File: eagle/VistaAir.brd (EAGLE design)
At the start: 97.3 x 54.6 mm, 12 parts

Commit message: fix manual routing short
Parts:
- moved B3 1.24 mm to (67.8, 36.2)
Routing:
- net BOARD_GND: track 148.1 -> 125.3 mm, vias 0 -> 2
- net 3V3: track 39.8 -> 41.6 mm
- net PWM1_5V: track 31.9 -> 30.6 mm
- net CLW2_5V: track 30.9 -> 29.7 mm
- net PWM2_5V: track 37.6 -> 36.4 mm
- net CLW1_5V: track 38.3 -> 37.1 mm
- net CLW2_3V3: track 9.40 -> 9.91 mm

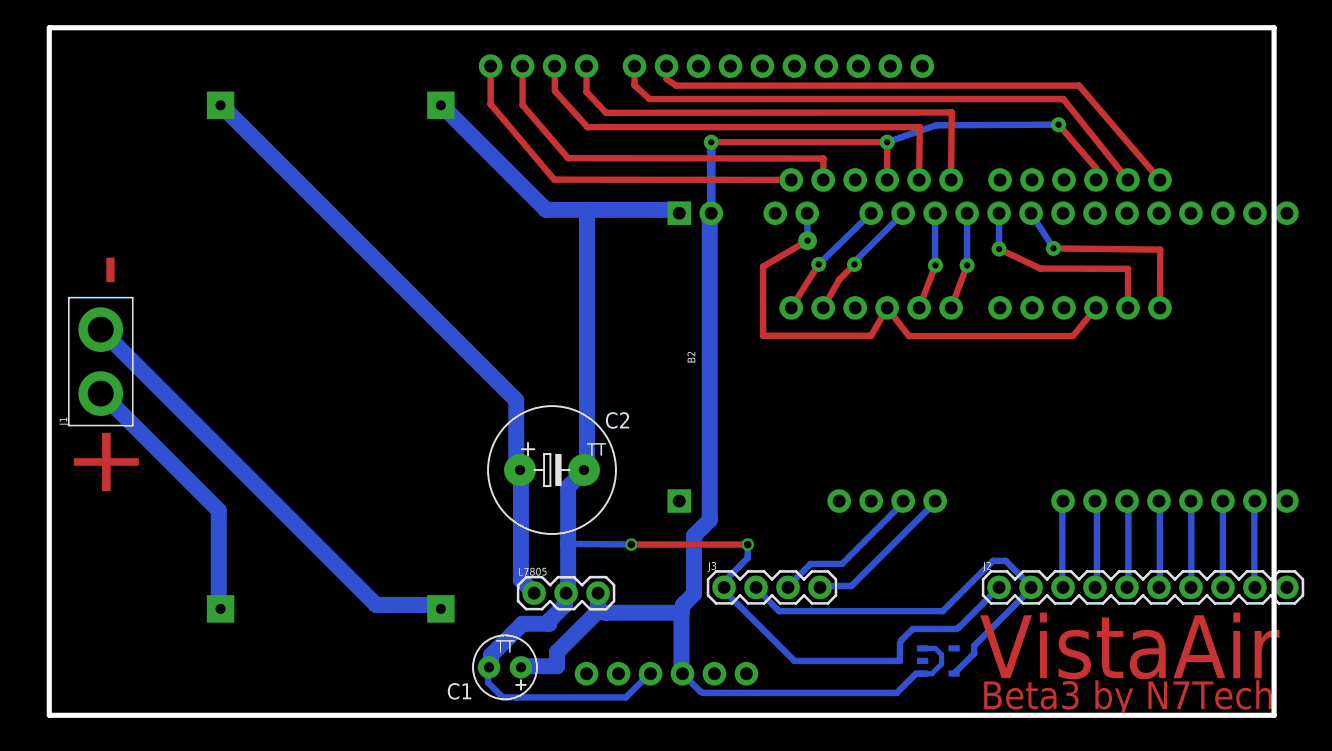
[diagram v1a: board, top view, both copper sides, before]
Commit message: managed to break ground connection to 3.6v regulator again - fixed it
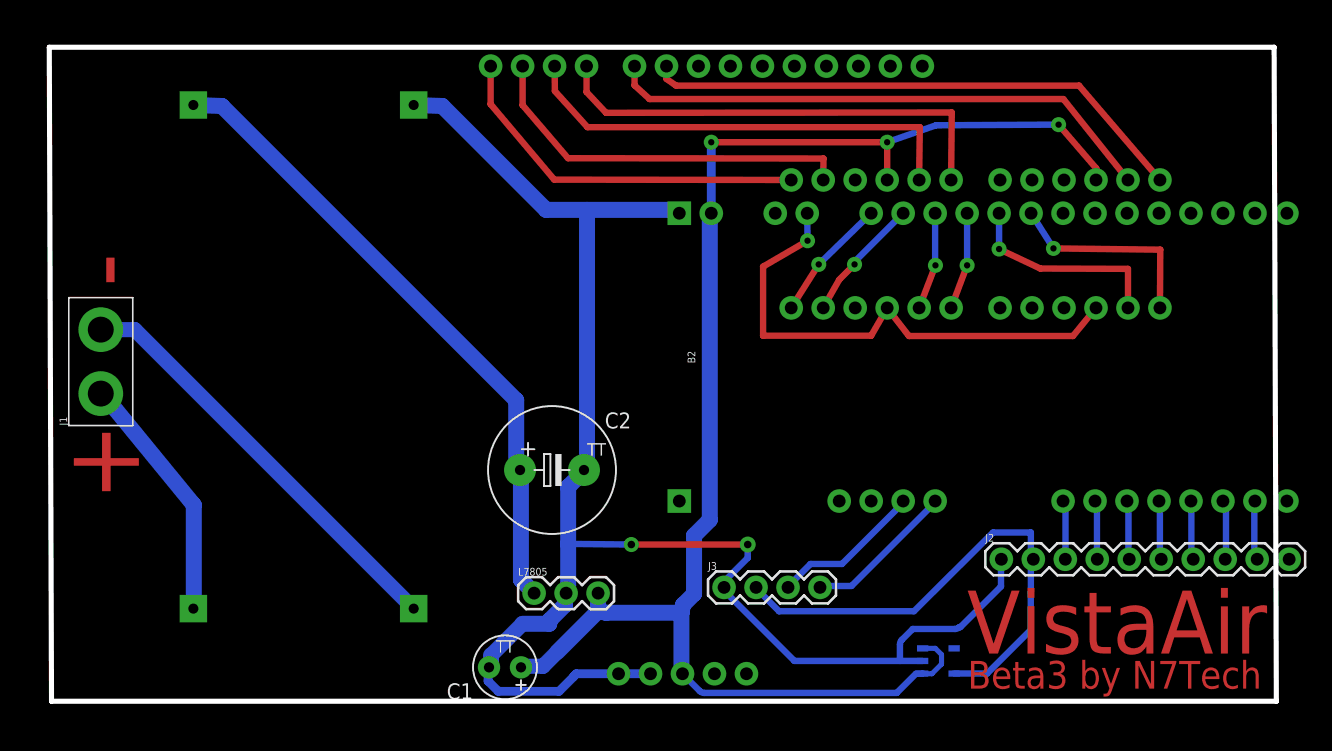
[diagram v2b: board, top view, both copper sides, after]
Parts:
- moved J2 2.24 mm to (78.2, 11.1)
- moved U$2 2.16 mm to (22.7, 27.2)
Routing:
- net 3V6: track 34.6 -> 40.7 mm
- net BOARD_GND: track 125.3 -> 131.4 mm
- net ENC1B: track 6.98 -> 4.67 mm
- net LIMTOPA: track 6.93 -> 4.66 mm
- net GND12: track 36.3 -> 34.0 mm
- net LIMTOPB: track 6.89 -> 4.67 mm
- net ENC1A: track 6.88 -> 4.69 mm
- net LIMBOTA: track 6.86 -> 4.69 mm
- net 5V5: track 49.0 -> 51.2 mm
- net LIMBOTB: track 6.86 -> 4.74 mm
- net LED: track 6.87 -> 4.76 mm
- net V12: track 21.0 -> 19.8 mm
- net V5IN: track 120.2 -> 119.6 mm
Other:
- board size 97.3 x 54.6 mm -> 97.5 x 51.9 mm

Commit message: board tidy up, encoders working with modified library
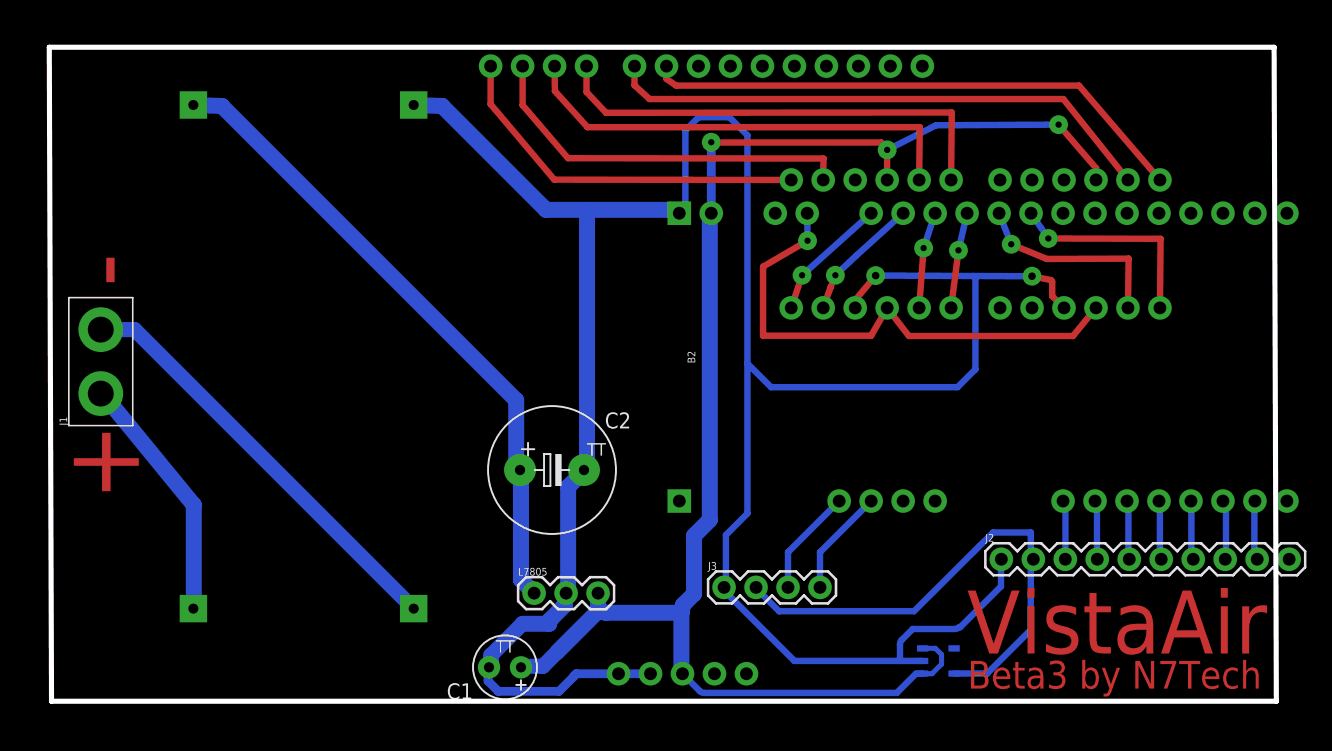
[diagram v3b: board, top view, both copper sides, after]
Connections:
- removed net N$1: B3.GND1
- removed net N$2: B3.GND2
- removed net N$3: B4.GND1
- removed net N$4: B4.GND2
- removed net NC1: B2.35
- removed net NC2: B2.34
- new net GND: B3.GND2, B4.GND2
- net BOARD_GND: now also B3.GND1, B4.GND1
- net ENC2A: now also B2.35; no longer B2.33
- net ENC2B: now also B2.34; no longer B2.32
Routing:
- net BOARD_GND: track 131.4 -> 209.0 mm
- net ENC2A: track 12.1 -> 8.54 mm
- net ENC2B: track 12.0 -> 8.54 mm

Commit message: board now with working logic converter
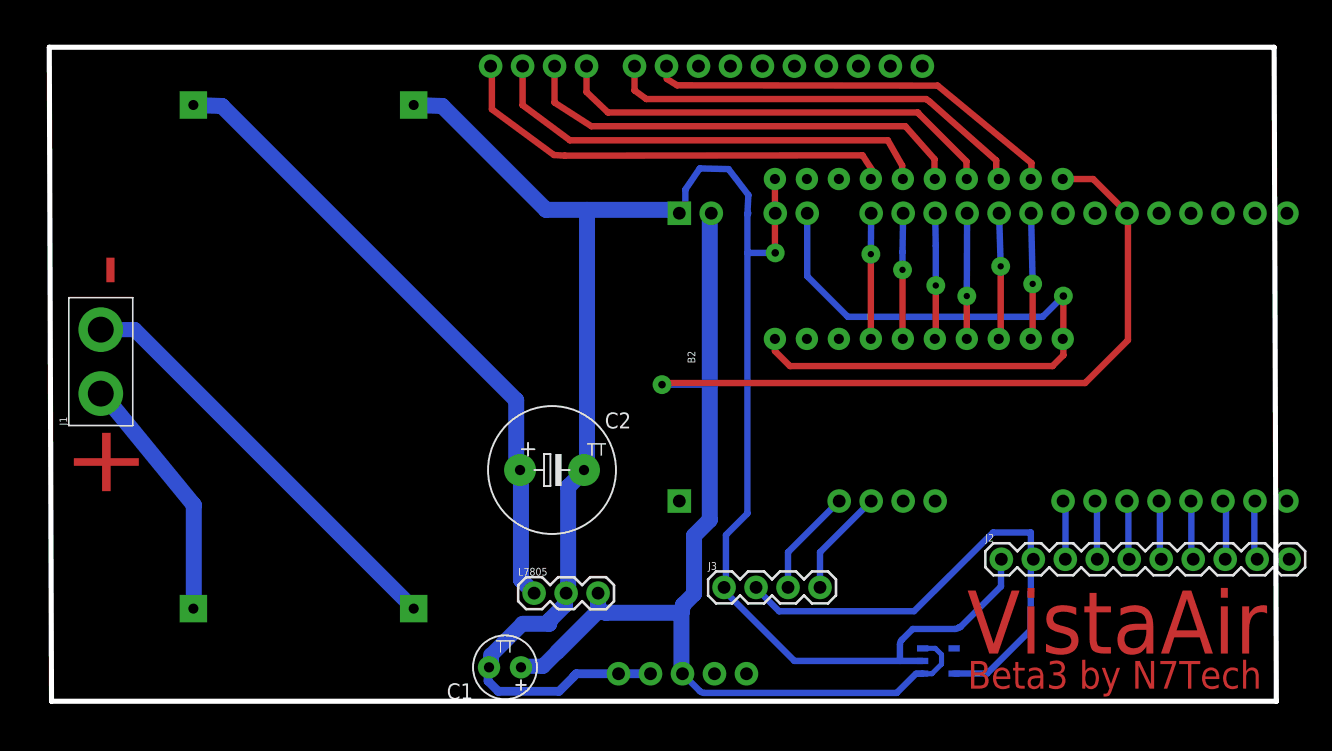
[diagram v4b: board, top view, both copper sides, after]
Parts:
- removed B3, B4: SPARKFUN_LOGIC_LEVEL_CONVERTER, SparkFun-Boards:SPARKFUN_LOGIC_LEVEL_CONVERTER
- added U$3: 8_CHANNEL_LOGIC_CONVERTER, kevins_parts:8_CHANNEL_LOGIC_CONVERTER
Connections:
- removed net GND: B3.GND2, B4.GND2
- net 3V3: now also U$3.OE, U$3.VA; no longer B3.LV, B4.LV
- net BOARD_GND: now also U$3.GND; no longer B3.GND1, B4.GND1
- net CCL1_3V3: now also U$3.A2; no longer B4.LV2
- net CCL1_5V: now also U$3.B2; no longer B4.HV2
- net CCL2_3V3: now also U$3.A1; no longer B4.LV1
- net CCL2_5V: now also U$3.B1; no longer B4.HV1
- net CLW1_3V3: now also U$3.A3; no longer B3.LV1
- net CLW1_5V: now also U$3.B3; no longer B3.HV1
- net CLW2_3V3: now also U$3.A6; no longer B3.LV4
- net CLW2_5V: now also U$3.B6; no longer B3.HV4
- net PWM1_3V3: now also U$3.A5; no longer B3.LV3
- net PWM1_5V: now also U$3.B5; no longer B3.HV3
- net PWM2_3V3: now also U$3.A4; no longer B3.LV2
- net PWM2_5V: now also U$3.B4; no longer B3.HV2
- net V5IN: now also U$3.VB; no longer B3.HV, B4.HV
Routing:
- net BOARD_GND: track 209.0 -> 162.1 mm, vias 2 -> 1
- net V5IN: track 119.5 -> 136.3 mm, vias 3 -> 1
- net 3V3: track 41.6 -> 56.8 mm
- net CCL2_5V: track 43.8 -> 33.6 mm
- net CCL1_5V: track 44.2 -> 34.3 mm
- net CCL2_3V3: track 16.8 -> 10.0 mm
- net CLW2_5V: track 29.7 -> 36.3 mm
- net CCL1_3V3: track 16.1 -> 10.0 mm
- net PWM1_5V: track 30.6 -> 36.4 mm
- net CLW1_3V3: track 7.63 -> 9.98 mm
- net PWM2_3V3: track 7.68 -> 10.0 mm
- net CLW1_5V: track 37.1 -> 35.9 mm

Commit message: still trying to get single power board to work with logic shifter - still failing
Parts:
- removed U$1: LDO_REGULATOR_LP2985-N, kevins_parts:LDO_REGULATOR_LP2985-N
- added IC1, IC2: MCP170312MB, linear:SOT89
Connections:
- removed net NC: U$1.BYPASS
- net 3V3: now also IC2.3; no longer B2.5
- net 3V6: now also IC1.3; no longer U$1.VOUT
- net BOARD_GND: now also IC1.1, IC2.1, J1.2; no longer U$1.GND
- net CCL1_3V3: now also B2.12; no longer B2.11
- net CCL2_3V3: now also B2.15; no longer B2.12
- net CLW1_3V3: now also B2.11; no longer B2.10
- net GND12: no longer J1.2
- net PWM1_3V3: now also B2.9; no longer B2.8
- net PWM2_3V3: now also B2.10; no longer B2.9
- net V5IN: now also IC1.2@1, IC2.2@1; no longer U$1.CNTRL, U$1.VIN
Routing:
- net GND12: track 34.0 -> 0.00 mm
- net BOARD_GND: track 162.1 -> 188.1 mm, vias 1 -> 2
- net 3V3: track 56.8 -> 31.9 mm, vias 1 -> 0
- net 3V6: track 40.7 -> 27.4 mm
- net CCL2_3V3: track 10.0 -> 14.1 mm
- net V5IN: track 136.3 -> 139.3 mm, vias 1 -> 6
- net CLW1_3V3: track 9.98 -> 11.0 mm
- net PWM1_3V3: track 9.99 -> 11.0 mm
- net PWM2_3V3: track 10.0 -> 11.0 mm
- net CCL1_3V3: track 10.0 -> 11.0 mm
- added copper zone on layer 1, net BOARD_GND
- added copper zone on layer 16, net BOARD_GND
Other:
- board size 97.5 x 51.9 mm -> 97.3 x 51.9 mm

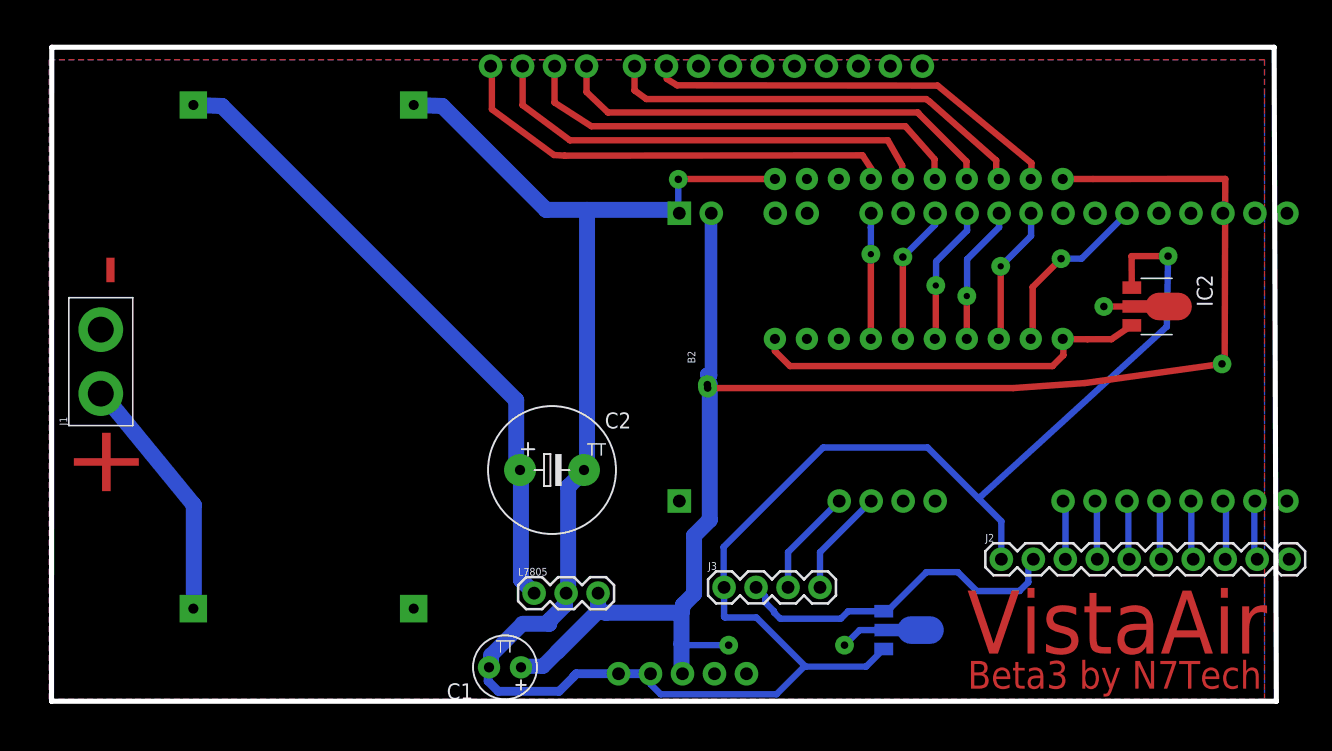
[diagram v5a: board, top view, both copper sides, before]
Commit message: barrel jack for board, fix pin numbers for arduino motor test and simplify board - diodes seem to be surplus to requirements. Logic shifting issue is something else
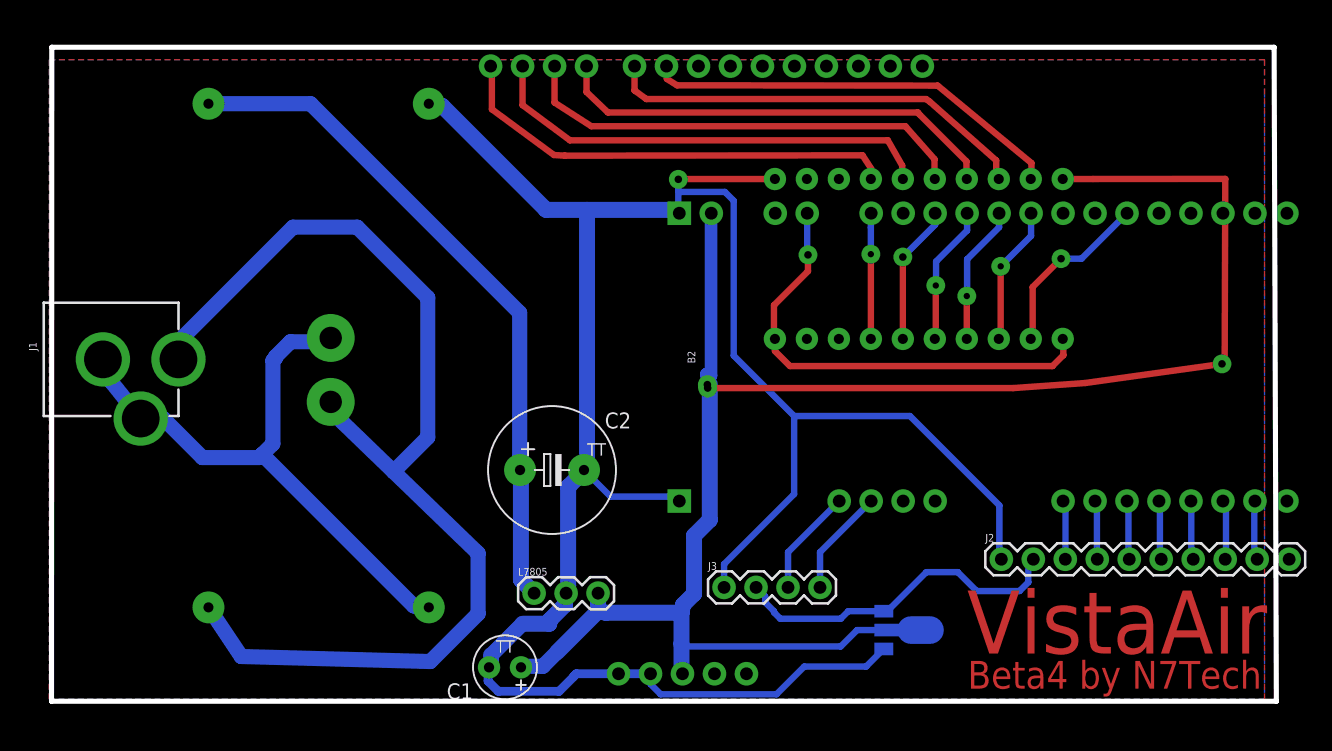
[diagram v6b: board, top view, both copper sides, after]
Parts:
- removed IC2: MCP170312MB, linear:SOT89
- J1: value (none) -> POWER_JACK; device SparkFun-Connectors:1X02_XTRA_BIG -> SparkFun-Connectors:POWER_JACK_PTH
- moved J1 7.53 mm to (-0.90, 27.0), turned to 270 degrees
- moved U$2 1.20 mm to (23.9, 27.3)
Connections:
- removed net GND12: U$2.GNDIN
- new net V12GND: B1.MAIN_GND, J1.GND, J1.GNDBREAK, U$2.GNDIN
- net 3V3: now also B2.5; no longer IC2.3
- net BOARD_GND: now also B1.BOARD_GND, B2.40; no longer B1.GND@0, IC2.1, J1.2
- net V12: now also B1.MAIN_VIN, J1.PWR; no longer J1.1
- net V5IN: no longer IC2.2@1
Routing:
- net V12: track 19.8 -> 89.2 mm
- net V12GND: track 0.00 -> 48.1 mm
- net 3V3: track 31.9 -> 37.2 mm, vias 0 -> 1
- net BOARD_GND: track 188.1 -> 183.3 mm, vias 2 -> 1
- net V5IN: track 139.3 -> 143.4 mm, vias 6 -> 3
- net 5V5: track 51.2 -> 54.3 mm
- added copper zone on layer 16, net BOTTOM_FILL
- added copper zone on layer 1, net TOP_FILL
- removed copper zone on layer 1, net BOARD_GND
- removed copper zone on layer 16, net BOARD_GND
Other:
- board text added: "Beta4 by N7Tech"
- board text removed: "+"
- board text removed: "-"
- board text removed: "Beta3 by N7Tech"
